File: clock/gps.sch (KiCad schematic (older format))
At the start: 9 parts

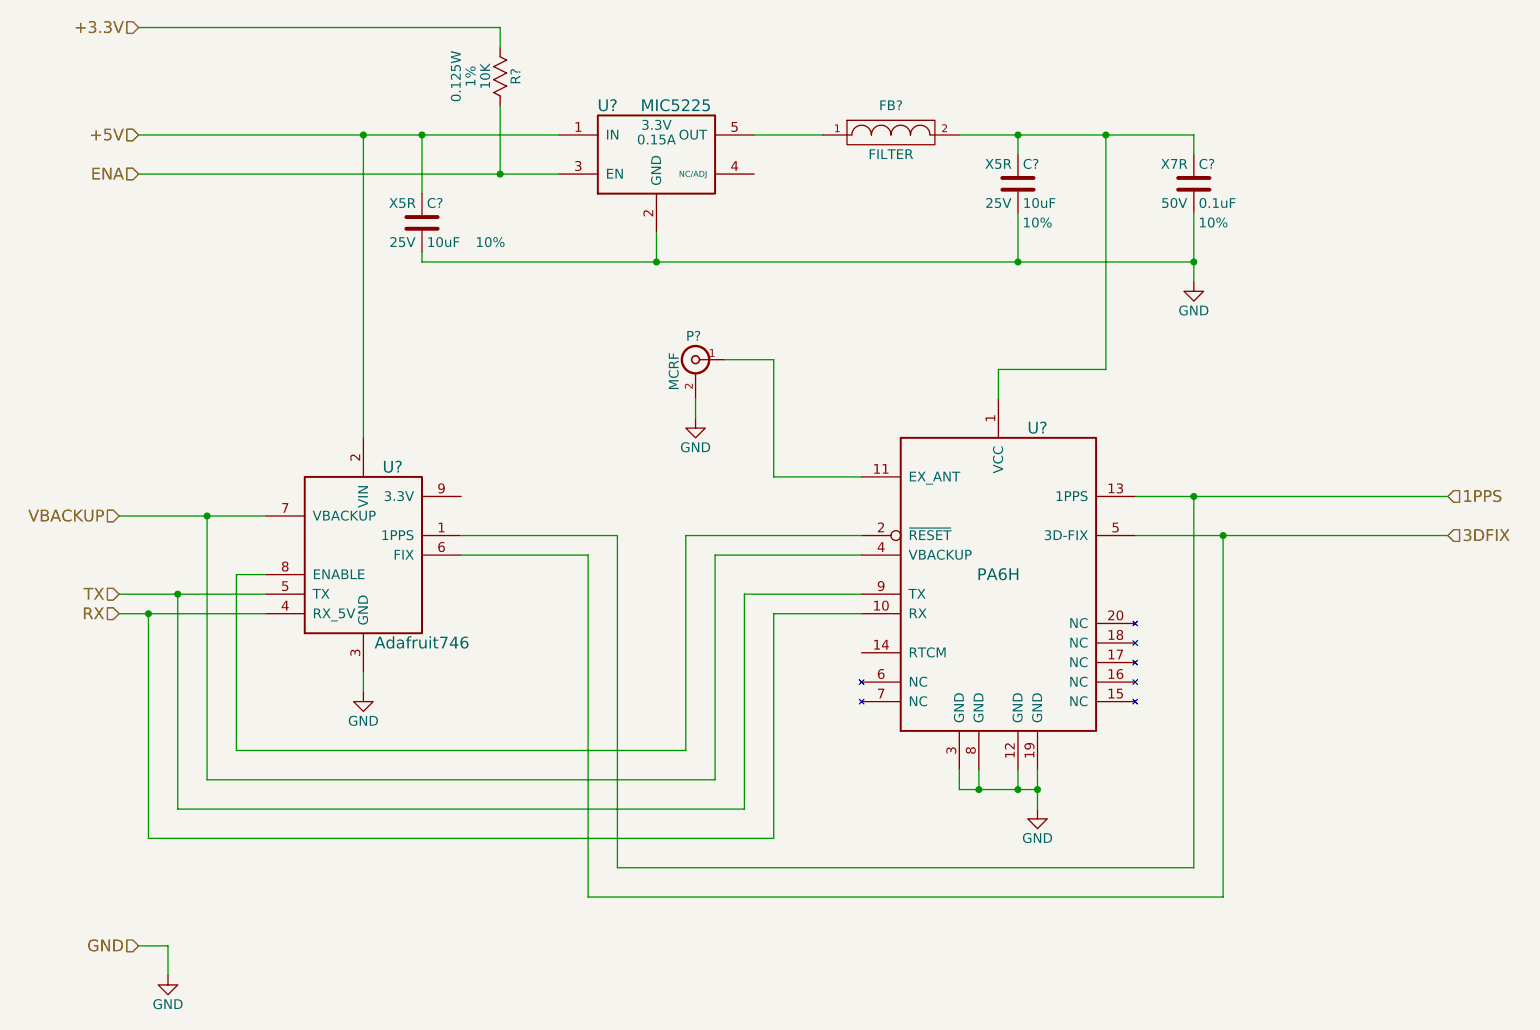
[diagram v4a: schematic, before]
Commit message: Correct footprint selection. Start pcb. Add BOM files.
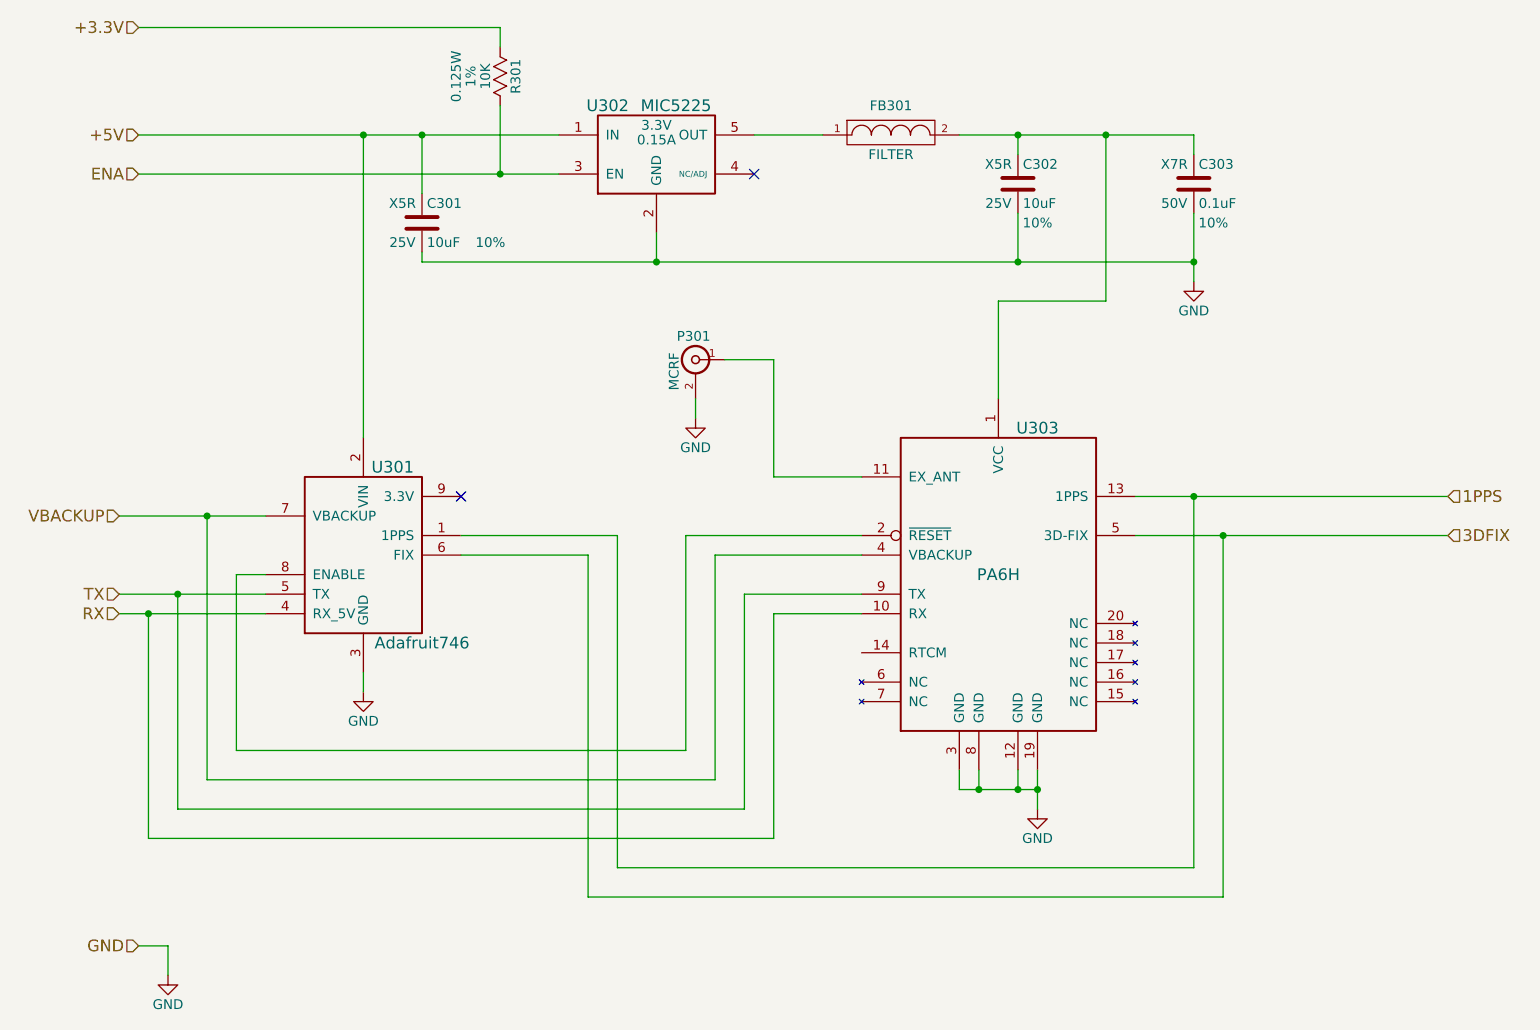
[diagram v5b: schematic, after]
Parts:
- FB301: renamed from FB?; footprint (none) -> Inductors_NEOSID:Neosid_Inductor_SM-NE45_SMD1812
- P301: renamed from P?; footprint (none) -> local:MCRF_73412
- U301: renamed from U?; footprint (none) -> local:Adafruit746
- U302: renamed from U?; footprint (none) -> local:SOT-23-5_1.6x2.9mm_Pitch0.95mm
- U303: renamed from U?; footprint (none) -> local:FGPMMOPA6H
- gave numbers to parts that had none: 4
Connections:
- no-connect marks 0 -> 2
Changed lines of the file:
@@
 $EndDescr
 $Comp
-L FILTER FB?
+L FILTER FB301
 U 1 1 561A31C6
 P 6450 1900
-F 0 "FB?" H 6450 2050 50  0000 C CNN
+F 0 "FB301" H 6450 2050 50  0000 C CNN
 F 1 "FILTER" H 6450 1800 50  0000 C CNN
-F 2 "" H 6450 1900 60  0000 C CNN
+F 2 "Inductors_NEOSID:Neosid_Inductor_SM-NE45_SMD1812" H 6450 1900 60  0001 C CNN
 F 3 "" H 6450 1900 60  0000 C CNN
 	1    6450 1900
@@
 $EndComp
 $Comp
-L BNC P?
+L BNC P301
 U 1 1 561A3335
 P 5450 3050
-F 0 "P?" H 5460 3170 50  0000 C CNN
+F 0 "P301" H 5460 3170 50  0000 C CNN
 F 1 "MCRF" V 5560 2990 50  0000 C CNN
-F 2 "" H 5450 3050 60  0000 C CNN
+F 2 "local:MCRF_73412" H 5450 3050 60  0001 C CNN
 F 3 "" H 5450 3050 60  0000 C CNN
 F 4 "Molex" H 5450 3050 50  0001 C CNN "Manufacturer"
@@
 $EndComp
 $Comp
-L GND #PWR?
+L GND #PWR046
 U 1 1 56235A8F
 P 7200 5350
-F 0 "#PWR?" H 7200 5100 50  0001 C CNN
+F 0 "#PWR046" H 7200 5100 50  0001 C CNN
 F 1 "GND" H 7200 5200 50  0000 C CNN
 F 2 "" H 7200 5350 60  0000 C CNN
@@
 Connection ~ 7100 1900
 $Comp
-L GND #PWR?
+L GND #PWR047
 U 1 1 56235D57
 P 8000 2650
-F 0 "#PWR?" H 8000 2400 50  0001 C CNN
+F 0 "#PWR047" H 8000 2400 50  0001 C CNN
 F 1 "GND" H 8000 2500 50  0000 C CNN
 F 2 "" H 8000 2650 60  0000 C CNN
@@
 	5850 3650 6300 3650
 $Comp
-L GND #PWR?
+L GND #PWR048
 U 1 1 56236310
 P 5450 3350
-F 0 "#PWR?" H 5450 3100 50  0001 C CNN
+F 0 "#PWR048" H 5450 3100 50  0001 C CNN
 F 1 "GND" H 5450 3200 50  0000 C CNN
 F 2 "" H 5450 3350 60  0000 C CNN
@@
 	2500 3850 3250 3850
 $Comp
-L GND #PWR?
+L GND #PWR049
 U 1 1 56236487
 P 3750 4750
-F 0 "#PWR?" H 3750 4500 50  0001 C CNN
+F 0 "#PWR049" H 3750 4500 50  0001 C CNN
 F 1 "GND" H 3750 4600 50  0000 C CNN
 F 2 "" H 3750 4750 60  0000 C CNN
@@
 Connection ~ 3750 1900
 Wire Wire Line
-	7000 3250 7000 3100
-Wire Wire Line
-	7000 3100 7550 3100
-Wire Wire Line
-	7550 3100 7550 1900
+	7000 3250 7000 2750
+Wire Wire Line
+	7000 2750 7550 2750
+Wire Wire Line
+	7550 2750 7550 1900
 Wire Wire Line
 	8000 1900 8000 2000
@@
 GND
 $Comp
-L GND #PWR?
+L GND #PWR050
 U 1 1 5624967B
 P 2750 6200
-F 0 "#PWR?" H 2750 5950 50  0001 C CNN
+F 0 "#PWR050" H 2750 5950 50  0001 C CNN
 F 1 "GND" H 2750 6050 50  0000 C CNN
 F 2 "" H 2750 6200 60  0000 C CNN
@@
 	2750 6050 2600 6050
 $Comp
-L C C?
+L C C302
 U 1 1 5631FA60
 P 7100 2150
-F 0 "C?" H 7125 2250 50  0000 L CNN
+F 0 "C302" H 7125 2250 50  0000 L CNN
 F 1 "10uF" H 7125 2050 50  0000 L CNN
 F 2 "Capacitors_SMD:C_1206_HandSoldering" H 7138 2000 30  0001 C CNN
@@
 $EndComp
 $Comp
-L C C?
+L C C303
 U 1 1 5631FA6C
 P 8000 2150
-F 0 "C?" H 8025 2250 50  0000 L CNN
+F 0 "C303" H 8025 2250 50  0000 L CNN
 F 1 "0.1uF" H 8025 2050 50  0000 L CNN
 F 2 "Capacitors_SMD:C_0805_HandSoldering" H 8038 2000 30  0001 C CNN
@@
 $EndComp
 $Comp
-L C C?
+L C C301
 U 1 1 5631FD2B
 P 4050 2350
-F 0 "C?" H 4075 2450 50  0000 L CNN
+F 0 "C301" H 4075 2450 50  0000 L CNN
 F 1 "10uF" H 4075 2250 50  0000 L CNN
 F 2 "Capacitors_SMD:C_1206_HandSoldering" H 4088 2200 30  0001 C CNN
@@
 $EndComp
 $Comp
-L MIC5225 U?
+L MIC5225 U302
 U 1 1 563293EE
 P 5250 2000
-F 0 "U?" H 5000 2250 60  0000 C CNN
+F 0 "U302" H 5000 2250 60  0000 C CNN
 F 1 "MIC5225" H 5350 2250 60  0000 C CNN
-F 2 "" H 5050 2000 60  0000 C CNN
+F 2 "local:SOT-23-5_1.6x2.9mm_Pitch0.95mm" H 5050 2000 60  0001 C CNN
 F 3 "" H 5050 2000 60  0000 C CNN
 F 4 "3.3V" H 5250 2150 50  0000 C CNN "Voltage"
@@
 $EndComp
 $Comp
-L Adafruit746 U?
+L Adafruit746 U301
 U 1 1 563295A6
 P 3750 4050
-F 0 "U?" H 3900 4500 60  0000 C CNN
+F 0 "U301" H 3900 4500 60  0000 C CNN
 F 1 "Adafruit746" H 4050 3600 60  0000 C CNN
-F 2 "" H 3750 4050 60  0000 C CNN
+F 2 "local:Adafruit746" H 3750 4050 60  0001 C CNN
 F 3 "" H 3900 4500 60  0000 C CNN
 F 4 "Adafruit" H 3950 3525 50  0001 C CNN "Manufacturer"
@@
 $EndComp
 $Comp
-L PA6H U?
+L PA6H U303
 U 1 1 56329634
 P 7000 4150
-F 0 "U?" H 7200 4900 60  0000 C CNN
+F 0 "U303" H 7200 4900 60  0000 C CNN
 F 1 "PA6H" H 7000 4150 60  0000 C CNN
-F 2 "" H 7500 4150 60  0000 C CNN
+F 2 "local:FGPMMOPA6H" H 7500 4150 60  0001 C CNN
 F 3 "" H 7500 4150 60  0000 C CNN
 F 4 "GlobalTop Technology" H 7000 4475 50  0001 C CNN "Manufacturer"
@@
 	3100 4150 3250 4150
 $Comp
-L R_local R?
+L R_local R301
 U 1 1 5632AC0C
 P 4450 1600
-F 0 "R?" V 4530 1600 50  0000 C CNN
+F 0 "R301" V 4530 1600 50  0000 C CNN
 F 1 "10K" V 4375 1600 50  0000 C CNN
 F 2 "Resistors_SMD:R_0805_HandSoldering" V 4380 1600 30  0001 C CNN
@@
 	1    0    0    -1
 $EndComp
+NoConn ~ 5750 2100
+NoConn ~ 4250 3750
 $EndSCHEMATC

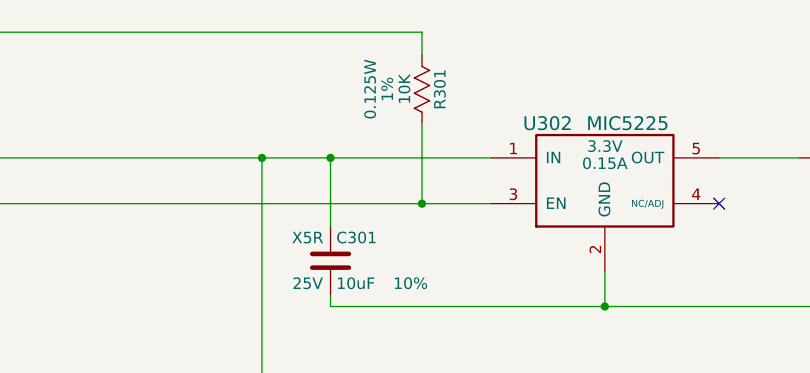
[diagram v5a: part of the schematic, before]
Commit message: Make component parameters consistent for BOM.
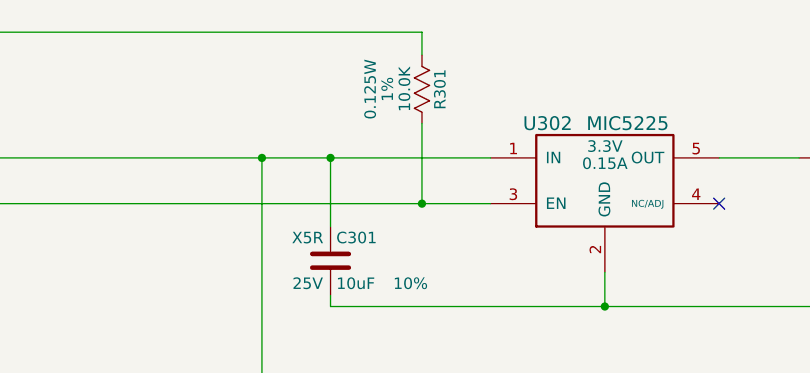
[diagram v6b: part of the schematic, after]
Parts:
- R301: value 10K -> 10.0K
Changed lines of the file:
@@
 P 4450 1600
 F 0 "R301" V 4530 1600 50  0000 C CNN
-F 1 "10K" V 4375 1600 50  0000 C CNN
+F 1 "10.0K" V 4375 1600 50  0000 C CNN
 F 2 "Resistors_SMD:R_0805_HandSoldering" V 4380 1600 30  0001 C CNN
 F 3 "" V 4530 1600 30  0000 C CNN

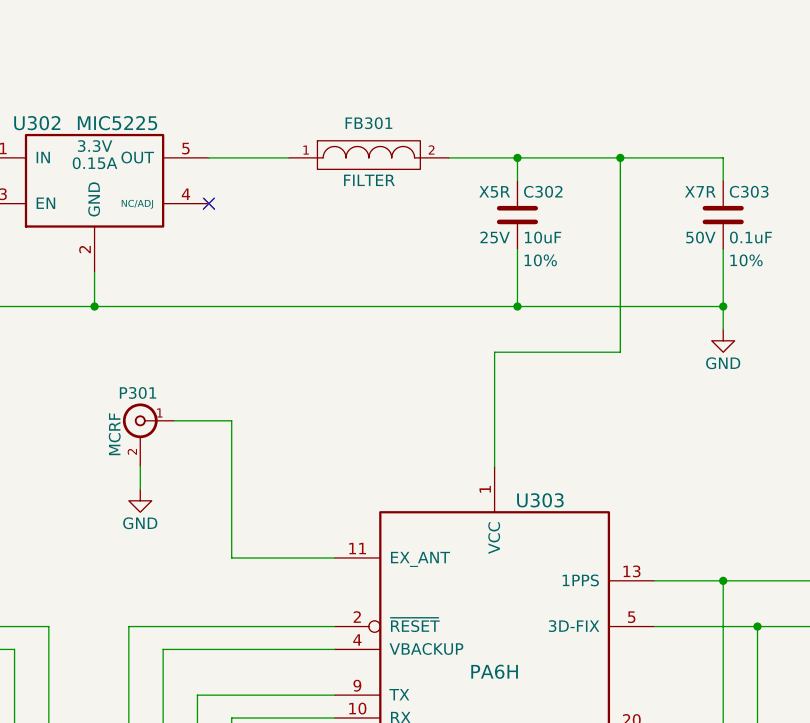
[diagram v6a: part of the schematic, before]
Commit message: Add net names to most of the nets.
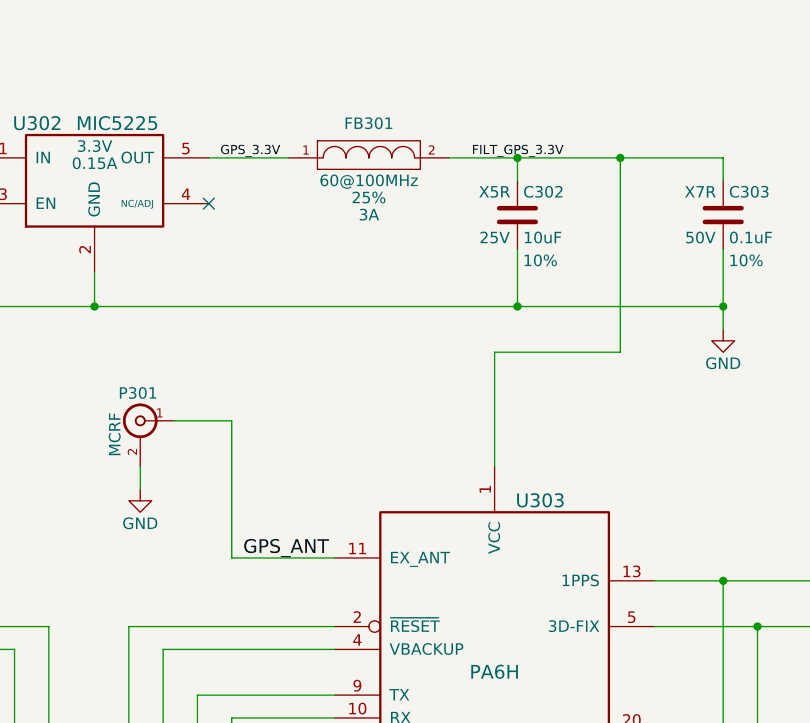
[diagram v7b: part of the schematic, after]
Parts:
- FB301: value FILTER -> 60@100MHz; footprint Inductors_NEOSID:Neosid_Inductor_SM-NE45_SMD1812 -> Resistors_SMD:R_0805_HandSoldering; Current (none) -> 3A; Manufacturer (none) -> Pulse Electronics; PartNum (none) -> PE-0805PFB600ST; Tolerance (none) -> 25%
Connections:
- net GPS_3.3V: now reaches FB301.1, U302.5 (OUT)
- net FILT_GPS_3.3V: now reaches C302.1, C303.1, FB301.2, U303.1 (VCC)
- net GPS_ANT: now reaches P301.1 (In), U303.11 (EX_ANT)
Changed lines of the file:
@@
 P 6450 1900
 F 0 "FB301" H 6450 2050 50  0000 C CNN
-F 1 "FILTER" H 6450 1800 50  0000 C CNN
-F 2 "Inductors_NEOSID:Neosid_Inductor_SM-NE45_SMD1812" H 6450 1900 60  0001 C CNN
+F 1 "60@100MHz" H 6450 1800 50  0000 C CNN
+F 2 "Resistors_SMD:R_0805_HandSoldering" H 6450 1900 60  0001 C CNN
 F 3 "" H 6450 1900 60  0000 C CNN
+F 4 "3A" H 6450 1650 50  0000 C CNN "Current"
+F 5 "25%" H 6450 1725 50  0000 C CNN "Tolerance"
+F 6 "Pulse Electronics" H 6450 1900 60  0001 C CNN "Manufacturer"
+F 7 "PE-0805PFB600ST" H 6450 1900 60  0001 C CNN "PartNum"
 	1    6450 1900
 	1    0    0    -1
@@
 NoConn ~ 5750 2100
 NoConn ~ 4250 3750
+Text Label 5900 3650 0    60   ~ 0
+GPS_ANT
+Text Label 5800 1900 0    40   ~ 0
+GPS_3.3V
+Text Label 6900 1900 0    40   ~ 0
+FILT_GPS_3.3V
 $EndSCHEMATC
